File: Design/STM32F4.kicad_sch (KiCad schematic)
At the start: 0 parts

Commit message: schematic updates
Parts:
- added JP? (x2): bit0, symbol Jumper:Jumper_2_Open
- added M?: STM32F4-DISCOVERY, STM32F4-DISCOVERY-SIMON_STM32F4-DISCOVERY, symbol STM32F4-DISCOVERY:STM32F4-DISCOVERY
- added R? (x2): 10k, symbol Device:R_Small
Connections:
- new net +3.3V: JP?.1 (A), JP?.1 (A)
- new net +5V: M?.53 (5V), M?.54 (5V2)
- new net AN_IN_VBatt: M?.11 (PA1)
- new net CANRX: M?.86 (PD0)
- new net CANTX: M?.83 (PD1)
- new net GND: M?.1 (GND), M?.100 (GND9), M?.2 (GND1), M?.49 (GND4), M?.5 (GND2), M?.50 (GND5), M?.51 (GND6), M?.52 (GND7), M?.99 (GND8), R?.2, R?.2
- new net HALLA: M?.75 (PB4)
- new net HALLB: M?.76 (PB5)
- new net HALLC: M?.22 (PB0)
- new net HS_A_TTL: M?.27 (PE9)
- new net HS_B_TTL: M?.29 (PE11)
- new net HS_C_TTL: M?.31 (PE13)
- new net LS_A_TTL: M?.26 (PE8)
- new net LS_B_TTL: M?.28 (PE10)
- new net LS_C_TTL: M?.30 (PE12)
- new net MOTOR_TEMP: M?.10 (PC2)
- new net PHASEA_FB: M?.20 (PC4)
- new net PHASEB_FB: M?.19 (PC5)
- new net PHASEC_FB: M?.7 (PC1)
- new net SA0: JP?.2 (B), R?.1
- new net SA1: JP?.2 (B), R?.1
- no-connect marks 0 -> 73
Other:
- note added: "Bit 0 = SA0, Bit 1 = SA1 0b00 (SOURCE ADDRESS = 0) 0b01 (SOURCE ADDRESS = 1) 0b10 (SOURCE ADDRESS = 2) 0b11 (SOURCE ADDRESS = 3)"
- note added: "SELECTABLE CAN SOURCE ADDRESS"
- note added: "STM32F4-Discovery uses 2x25 0.1" female headers on each side PN: SAM10038-ND"

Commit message: MOSFETS
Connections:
- net +5V: no longer names the net of M?.53 (5V)
- net +5V: no longer M?.54 (5V2)
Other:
- note added: "MUST FIGURE OUT 3.3V POWER SITUATION"
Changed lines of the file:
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@@
     (stroke (width 0) (type default) (color 0 0 0 0))
+  )
+  (text "MUST FIGURE OUT 3.3V POWER SITUATION" (at 153.035 57.15 0)
+    (effects (font (size 1.27 1.27)) (justify left bottom))
   )
   (text "Bit 0 = SA0, Bit 1 = SA1\n0b00 (SOURCE ADDRESS = 0)\n0b01 (SOURCE ADDRESS = 1)\n0b10 (SOURCE ADDRESS = 2)\n0b11 (SOURCE ADDRESS = 3)"
@@
     (pin "2")
   )
-  (symbol (lib_id "power:+5V") (at 203.2 63.5 90) (unit 1)
-    (in_bom yes) (on_board yes)
-    (property "Reference" "#PWR5" (id 0) (at 207.01 63.5 0)
-      (effects (font (size 1.27 1.27)) hide)
-    )
-    (property "Value" "+5V" (id 1) (at 196.215 63.5 90)
-      (effects (font (size 1.27 1.27)) (justify right))
-    )
-    (property "Footprint" "" (id 2) (at 203.2 63.5 0)
-      (effects (font (size 1.27 1.27)) hide)
-    )
-    (property "Datasheet" "" (id 3) (at 203.2 63.5 0)
-      (effects (font (size 1.27 1.27)) hide)
-    )
-    (pin "1")
-  )
   (symbol (lib_id "power:+3.3V") (at 36.83 69.85 0) (unit 1)
     (in_bom yes) (on_board yes) (fields_autoplaced)
@@
       (effects (font (size 1.27 1.27)) hide)
     )
-    (pin "1")
-  )
-  (symbol (lib_id "power:+5V") (at 233.68 63.5 270) (unit 1)
-    (in_bom yes) (on_board yes)
-    (property "Reference" "#PWR5" (id 0) (at 229.87 63.5 0)
-      (effects (font (size 1.27 1.27)) hide)
-    )
-    (property "Value" "+5V" (id 1) (at 236.22 63.5 90)
-      (effects (font (size 1.27 1.27)) (justify left))
-    )
-    (property "Footprint" "" (id 2) (at 233.68 63.5 0)
-      (effects (font (size 1.27 1.27)) hide)
-    )
-    (property "Datasheet" "" (id 3) (at 233.68 63.5 0)
-      (effects (font (size 1.27 1.27)) hide)
-    )

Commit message: Micro update
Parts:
- removed M?: STM32F4-DISCOVERY, STM32F4-DISCOVERY-SIMON_STM32F4-DISCOVERY, symbol STM32F4-DISCOVERY:STM32F4-DISCOVERY
- added C? (x8): 100n, symbol Device:C_Small
- added C? (x4): 2.2u, symbol Device:C_Small
- added C? (x2): 20p, symbol Device:C
- added R? (x3): 39k, symbol Device:R
- added R? (x3): 2.2k, symbol Device:R
- added U?: STM32F407VGTx, Package_QFP:LQFP-100_14x14mm_P0.5mm, symbol MCU_ST_STM32F4:STM32F407VGTx
- added Y?: 8M, symbol Device:Crystal_GND3
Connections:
- net +3.3V: now also C?.1, C?.1, C?.1, C?.1, C?.1, C?.1, C?.1, C?.1, C?.1, U?.100 (VDD), U?.11 (VDD), U?.19 (VDD), U?.21 (VREF+), U?.22 (VDDA), U?.28 (VDD), U?.50 (VDD), U?.6 (VBAT), U?.75 (VDD)
- net AN_IN_VBatt: now also U?.34 (PC5)
- net CANRX: now also U?.81 (PD0)
- net CANTX: now also U?.82 (PD1)
- net GND: now also C?.1, C?.1, C?.2, C?.2, C?.2, C?.2, C?.2, C?.2, C?.2, C?.2, C?.2, C?.2, C?.2, C?.2, R?.2, R?.2, R?.2, U?.10 (VSS), U?.20 (VSSA), U?.27 (VSS), U?.74 (VSS), U?.94 (BOOT0), U?.99 (VSS), Y?.3
- net HALLA: now also U?.90 (PB4)
- net HALLB: now also U?.91 (PB5)
- net HALLC: now also U?.35 (PB0)
- net HS_A_TTL: now also U?.40 (PE9)
- net HS_B_TTL: now also U?.42 (PE11)
- net HS_C_TTL: now also U?.44 (PE13)
- net LS_A_TTL: now also U?.39 (PE8)
- net LS_B_TTL: now also U?.41 (PE10)
- net LS_C_TTL: now also U?.43 (PE12)
- net MOTOR_TEMP: now also U?.33 (PC4)
- net PHASEA_FB: now also U?.15 (PC0)
- net PHASEB_FB: now also U?.16 (PC1)
- net PHASEC_FB: now also U?.17 (PC2)
- new net: C?.1, U?.12 (PH0), Y?.1
- new net: C?.1, U?.13 (PH1), Y?.2
- new net: C?.2, U?.49 (VCAP_1)
- new net: C?.2, U?.73 (VCAP_2)
- new net NRST: C?.1, U?.14 (NRST)
- new net SENSE_A: R?.1, R?.1, U?.23 (PA0)
- new net SENSE_B: R?.1, R?.1, U?.24 (PA1)
- new net SENSE_C: R?.1, R?.1, U?.25 (PA2)
- new net VOLTAGE_A: R?.2
- new net VOLTAGE_B: R?.2
- new net VOLTAGE_C: R?.2
- no-connect marks 73 -> 61
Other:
- note added: "Bypass, place near VDD pins"
- note added: "CURRENT SENSE"
- note added: "VOLTAGE SENSE"
- note removed: "MUST FIGURE OUT 3.3V POWER SITUATION"
- note removed: "STM32F4-Discovery uses 2x25 0.1" female headers on each side PN: SAM10038-ND"
- moved on the sheet: JP?, R?

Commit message: 3.3v reg
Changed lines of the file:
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@@
   (symbol (lib_id "Device:C_Small") (at 108.585 52.705 270) (unit 1)
     (in_bom yes) (on_board yes)
-    (property "Reference" "C?" (id 0) (at 105.41 53.975 90))
-    (property "Value" "100n" (id 1) (at 111.76 53.975 90))
+    (property "Reference" "C?" (id 0) (at 110.49 53.975 90))
+    (property "Value" "100n" (id 1) (at 105.41 53.975 90))
     (property "Footprint" "" (id 2) (at 108.585 52.705 0)
       (effects (font (size 1.27 1.27)) hide)

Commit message: SWD debugger
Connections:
- net CAL: now reaches U?.36 (PB1)
- net nFAULT: now reaches U?.37 (PB2)
- net SWDIO: now reaches U?.72 (PA13)
- net SWCLK: now reaches U?.76 (PA14)
- net ENABLE: now reaches U?.89 (PB3)
- no-connect marks 61 -> 56
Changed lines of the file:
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@@
   (no_connect (at 117.475 157.48))
   (no_connect (at 117.475 116.84))
-  (no_connect (at 163.195 71.12))
   (no_connect (at 117.475 149.86))
   (no_connect (at 117.475 129.54))
@@
   (no_connect (at 163.195 96.52))
   (no_connect (at 163.195 109.22))
-  (no_connect (at 163.195 81.28))
   (no_connect (at 163.195 43.18))
   (no_connect (at 117.475 96.52))
@@
   (no_connect (at 163.195 160.02))
   (no_connect (at 163.195 48.26))
-  (no_connect (at 163.195 86.36))
   (no_connect (at 163.195 114.3))
   (no_connect (at 163.195 139.7))
@@
   (no_connect (at 117.475 81.28))
   (no_connect (at 163.195 45.72))
-  (no_connect (at 163.195 83.82))
   (no_connect (at 163.195 149.86))
   (no_connect (at 163.195 60.96))
@@
   (no_connect (at 163.195 93.98))
   (no_connect (at 117.475 137.16))
-  (no_connect (at 163.195 68.58))
   (wire (pts (xy 203.2 56.515) (xy 203.2 59.69))
     (stroke (width 0) (type default) (color 0 0 0 0))
@@
     (effects (font (size 1.27 1.27)) (justify left))
   )
+  (hierarchical_label "CAL" (shape output) (at 163.195 81.28 0)
+    (effects (font (size 1.27 1.27)) (justify left))
+  )
   (hierarchical_label "PHASEB_FB" (shape input) (at 163.195 124.46 0)
     (effects (font (size 1.27 1.27)) (justify left))
@@
     (effects (font (size 1.27 1.27)) (justify left))
   )
+  (hierarchical_label "nFAULT" (shape input) (at 163.195 83.82 0)
+    (effects (font (size 1.27 1.27)) (justify left))
+  )
   (hierarchical_label "PHASEA_FB" (shape input) (at 163.195 121.92 0)
     (effects (font (size 1.27 1.27)) (justify left))
@@
     (effects (font (size 1.27 1.27)) (justify right))
   )
+  (hierarchical_label "SWCLK" (shape input) (at 163.195 71.12 0)
+    (effects (font (size 1.27 1.27)) (justify left))
+  )
   (hierarchical_label "CANTX" (shape output) (at 117.475 124.46 180)
     (effects (font (size 1.27 1.27)) (justify right))
   )
+  (hierarchical_label "ENABLE" (shape output) (at 163.195 86.36 0)
+    (effects (font (size 1.27 1.27)) (justify left))
+  )
   (hierarchical_label "LS_A_TTL" (shape output) (at 117.475 99.06 180)
     (effects (font (size 1.27 1.27)) (justify right))
@@
     (effects (font (size 1.27 1.27)) (justify right))
   )
+  (hierarchical_label "SWDIO" (shape input) (at 163.195 68.58 0)
+    (effects (font (size 1.27 1.27)) (justify left))
+  )
   (hierarchical_label "LS_B_TTL" (shape output) (at 117.475 104.14 180)

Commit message: Updating schematic
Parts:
- JP2, JP3: renamed from JP?; value bit0 -> 0.1" Jumper
- gave numbers to parts that had none: 24
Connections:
- net CAL: now also U2.89 (PB3); no longer U2.36 (PB1)
- net ENABLE: now also U2.91 (PB5); no longer U2.89 (PB3)
- net HALLA: now also U2.37 (PB2); no longer U2.90 (PB4)
- net HALLB: now also U2.36 (PB1); no longer U2.91 (PB5)
- net nFAULT: now also U2.90 (PB4); no longer U2.37 (PB2)
- net USART_CTS: now reaches U2.52 (PB13)
- net USART_RTS: now reaches U2.53 (PB14)
- net USART_TX: now reaches U2.55 (PD8)
- net USART_RX: now reaches U2.56 (PD9)
- no-connect marks 56 -> 52

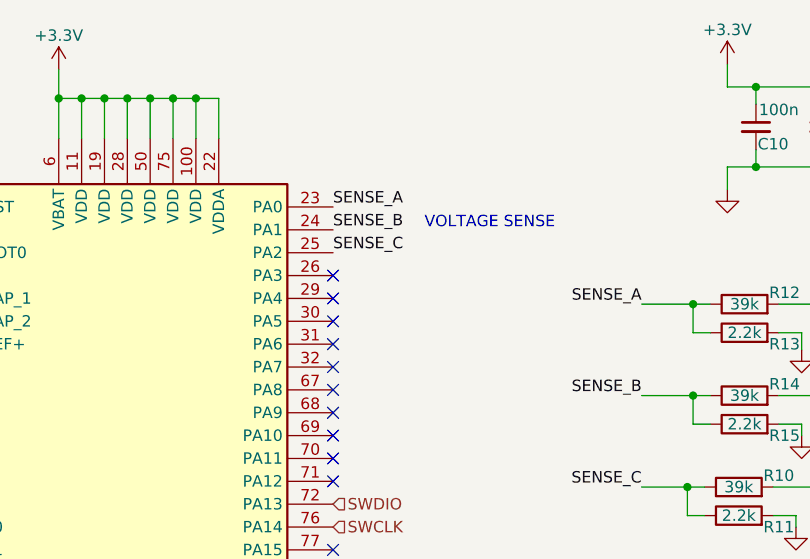
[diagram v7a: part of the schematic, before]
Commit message: adding caps
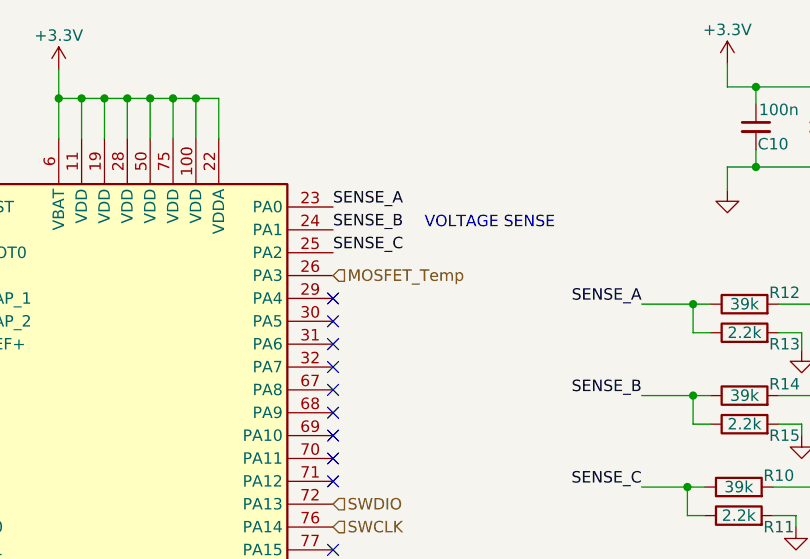
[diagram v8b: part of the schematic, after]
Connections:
- net MOSFET_Temp: now reaches U2.26 (PA3)
- no-connect marks 52 -> 51
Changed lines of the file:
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@@
   (no_connect (at 163.195 96.52))
   (no_connect (at 163.195 109.22))
-  (no_connect (at 163.195 43.18))
   (no_connect (at 117.475 96.52))
   (no_connect (at 117.475 154.94))
@@
     (effects (font (size 1.27 1.27)) (justify left))
   )
+  (hierarchical_label "MOSFET_Temp" (shape input) (at 163.195 43.18 0)
+    (effects (font (size 1.27 1.27)) (justify left))
+  )
